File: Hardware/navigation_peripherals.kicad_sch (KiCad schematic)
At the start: 30 parts, among them J2 5-1814832-1, J3 Conn_01x04, J4 Conn_01x04, J5 Conn_01x04, U10 BMP390, U11 W25N01GVZEIG_TR, U5 IST8310, U6 NEO-M8N, U7 BMI088, U8 TMP100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

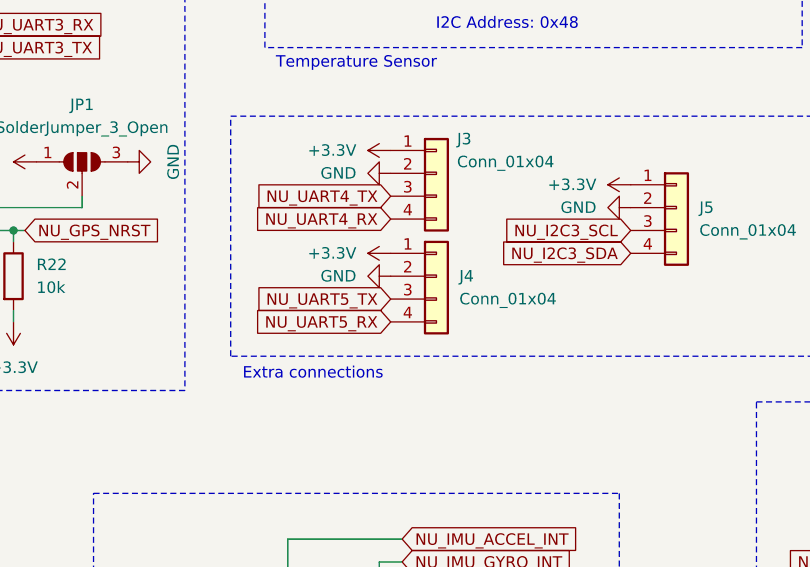
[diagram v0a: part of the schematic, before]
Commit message: fixed some errors in global labels
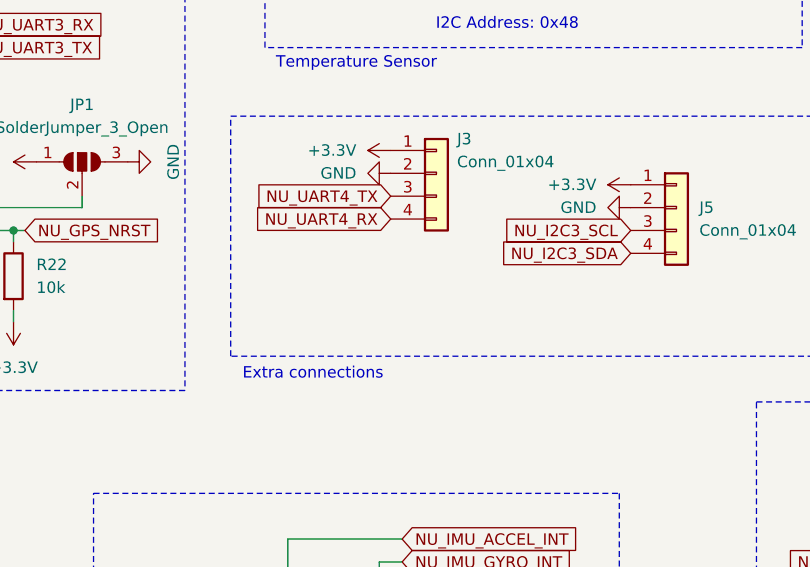
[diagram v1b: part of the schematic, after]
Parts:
- removed J4: Conn_01x04, symbol Connector_Generic:Conn_01x04
